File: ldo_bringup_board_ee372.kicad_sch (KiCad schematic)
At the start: 71 parts, among them J1 VIN, J10 MD_SW_EN, J13 V_SIG, J15 VSIG_BUF, J2 GND, J3 IBIAS, J4 VOUT, J5 VIN_SMA, J6 VOUT_SMA, J7 GND, J8 5V, Q1 FDV305N, Q2 FDV305N, Q3 FDV305N, Q4 FDV305N, Q5 FDV305N, SW1 SW_SPDT, U1 LDO_DualMode_BGR_EE372

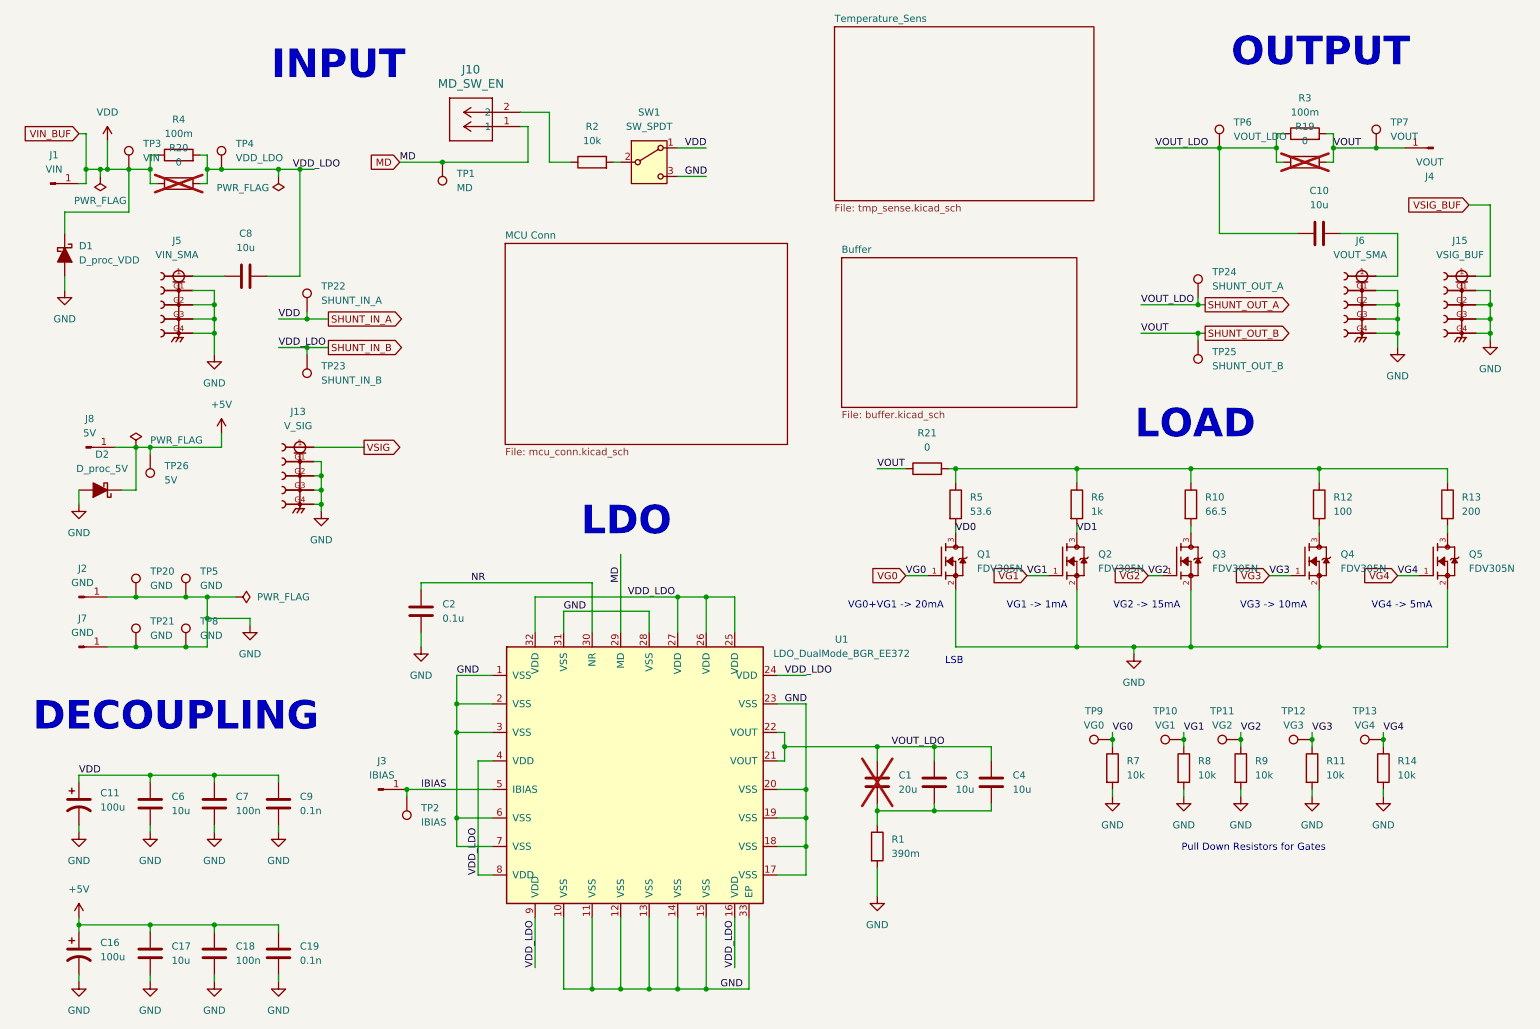
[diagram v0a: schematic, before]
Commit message: Finish the BUF602 buffer, add M3 mounting holes, direct-couple the SMAs
The netlist goes from 114 parts and 89 nets to 116 parts and 84 nets.
ERC shows 0 errors and 37 warnings.

Schematic edits by Luke
- Buffer sheet. ls1031's J16, J17 and J18 removed. The BUF602 (U6) now
  uses the top-sheet SMAs, J13 on its input (VSIG) and J14 on its output
  (VSIG_BUF, was J15), both now the edge-mount Samtec part. Its output
  reaches the chip's VDD pins through R34 (2.2 ohm) onto SHUNT_IN_B. V+
  comes from +5V through jumper J12 BUF_EN.
- The buffer's supply caps renumbered to C26 (4.7u) and C27 (0.1u), so
  C24 and C25 are the INA190 input filter caps again.
- C8 and C10 removed. J5 now connects directly to SHUNT_IN_B (VDD_LDO)
  and J6 directly to SHUNT_OUT_A (VOUT_LDO).
- Four mounting holes, H1 to H4.

Field edits by Claude
- U6 is the TI BUF602ID (tube; the BUF602IDR reel is obsolete at DigiKey).
- R34 footprint and part, Panasonic ERJ-6RQF2R2V.
- C26 and C27 part numbers changed to match their values (they carried a
  10 uF 10 V KEMET number), Samsung CL21B475KAFNNNE and CL21B104KBCNNNC.
- H1 to H4 footprint changed from the 2-pin header to
  MountingHole_3.2mm_M3, per the guidelines' four M3 holes.
Netlist exports before and after each field edit have identical nets.

Co-Authored-By: Claude Opus 5.5 (1M context) <noreply@anthropic.com>
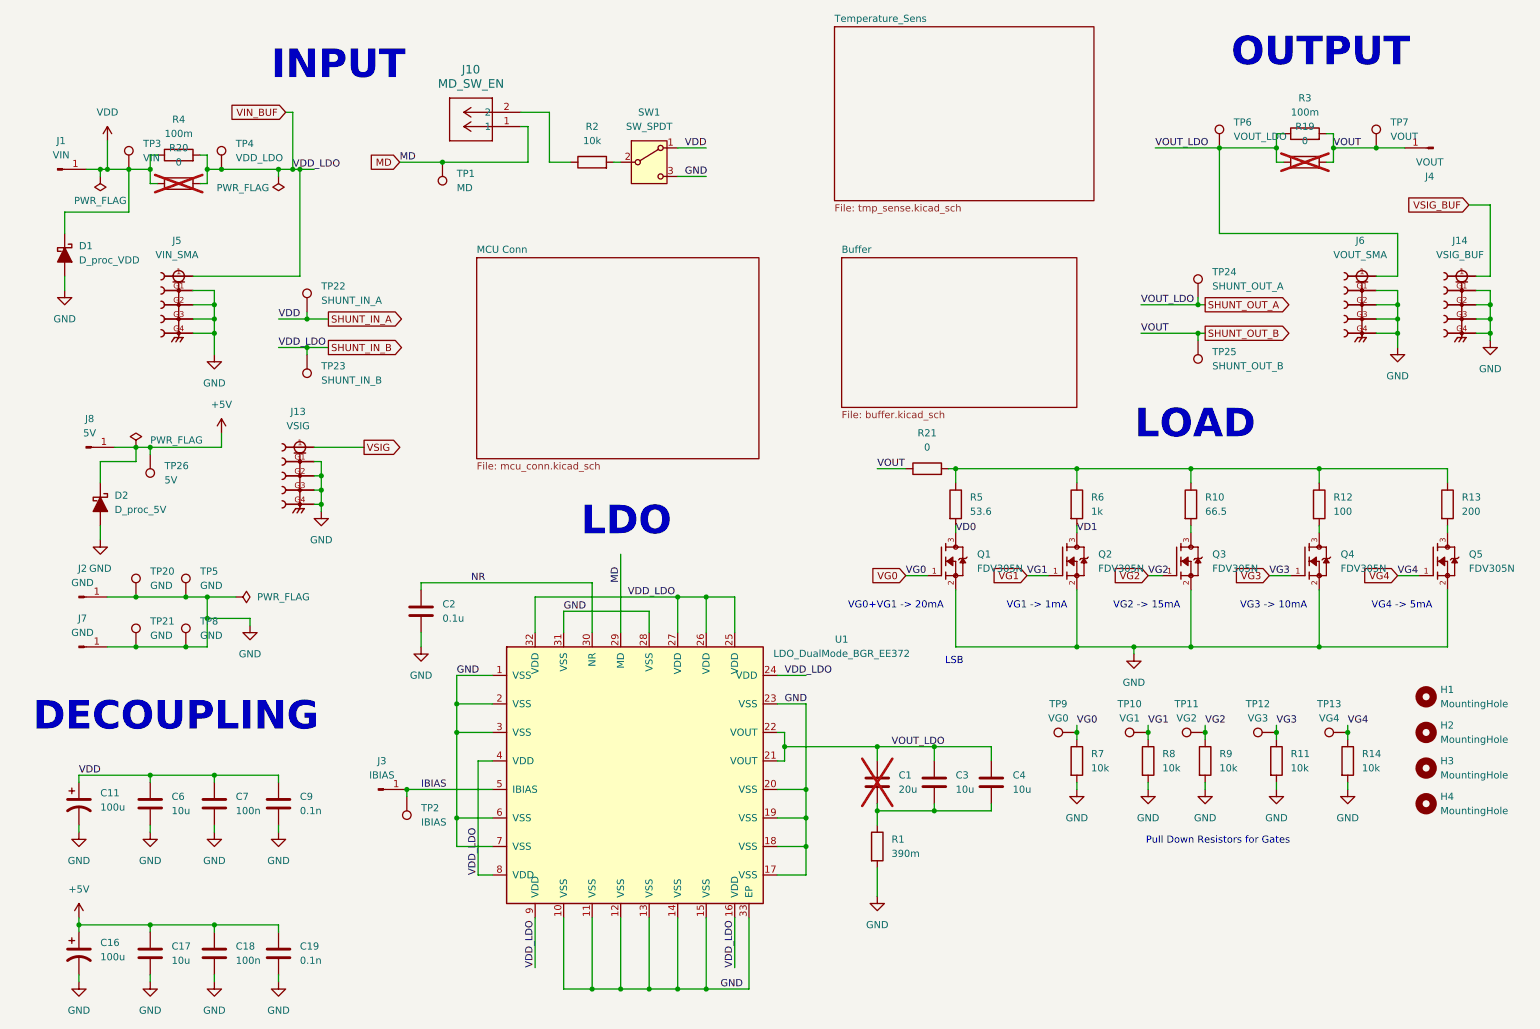
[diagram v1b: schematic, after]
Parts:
- removed C10, C8: 10u, Capacitor_SMD:C_1206_3216Metric_Pad1.33x1.80mm_HandSolder, symbol Device:C
- removed J13: V_SIG, TPS7A7001_Evaluation_Board_footprint_lib:SAMTEC_SMA-J-P-H-ST-TH1, symbol SMA-J-P-H-ST-TH1:SMA-J-P-H-ST-TH1
- removed J15: VSIG_BUF, SMA_J_P_H_ST_TH1:SAMTEC_SMA-J-P-H-ST-TH1, symbol SMA-J-P-H-ST-TH1:SMA-J-P-H-ST-TH1
- added H1, H2, H3, H4: MountingHole, MountingHole:MountingHole_3.2mm_M3, symbol Mechanical:MountingHole
- added J13: VSIG, ldo_bringup_board_ee372:SMA_Samtec_SMA-J-P-H-ST-EM1_EdgeMount_G, symbol ldo_bringup_board_ee372:SMA-J-P-H-ST-EM1
- added J14: VSIG_BUF, ldo_bringup_board_ee372:SMA_Samtec_SMA-J-P-H-ST-EM1_EdgeMount_G, symbol ldo_bringup_board_ee372:SMA-J-P-H-ST-EM1
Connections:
- net GND: now also J13.G1, J13.G2, J13.G3, J13.G4, J14.G1, J14.G2, J14.G3, J14.G4
- net SHUNT_IN_B: now also J5.1
- net SHUNT_OUT_A: now also J6.1
- net VSIG: now also J13.1
- net VSIG_BUF: now also J14.1
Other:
- moved on the sheet: J1, R11, R14, R7, R8, R9, TP10, TP11, TP12, TP13, TP9
